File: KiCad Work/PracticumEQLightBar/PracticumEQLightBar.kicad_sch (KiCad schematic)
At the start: 57 parts, among them J1 AudioJack3Pin, U1 TEENSY 4.1, U2 TEENSY AUDIO ADAPTER BOARD RE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, U4 SN74AHCT125N

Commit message: Added unified power, caps, Data in resistor. Modified placements to match enclosure I/O git status
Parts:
- removed TP1, TP2: TestPoint_Alt, TestPoint:TestPoint_Pad_1.5x1.5mm, symbol Connector:TestPoint_Alt
- added C1: 470u, Capacitor_THT:CP_Radial_D8.0mm_P3.80mm, symbol Device:C_Small_US
- added C2: 0.1u, Capacitor_THT:C_Disc_D4.7mm_W2.5mm_P5.00mm, symbol Device:C_Small
- added J2: 5V, 4A DC, EQLightBarLibrary:PJ047BH DC Jack, symbol Connector:Barrel_Jack_Switch
- added R1: 330, Resistor_THT:R_Axial_DIN0207_L6.3mm_D2.5mm_P7.62mm_Horizontal, symbol Device:R_Small
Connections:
- net 3.3V DATA: now also U4.2 (1A); no longer U4.5 (2A)
- net CLOCK: now also U4.5 (2A); no longer U4.2 (1A)
- net GND: now also U1.GND1 (GND), U1.GND3 (GND__2), U2.G, U2.GND, C1.2, C2.2, J2.2, J2.3
- net at D1.1 (DI): now also R1.2; no longer U4.6 (2Y)
- net at D1.2 (CI): now also U4.6 (2Y); no longer U4.3 (1Y)
- net 5V USB renamed 5V DC
- net 5V DC: now also C1.1, C2.1, J2.1
- new net: R1.1, U4.3 (1Y)

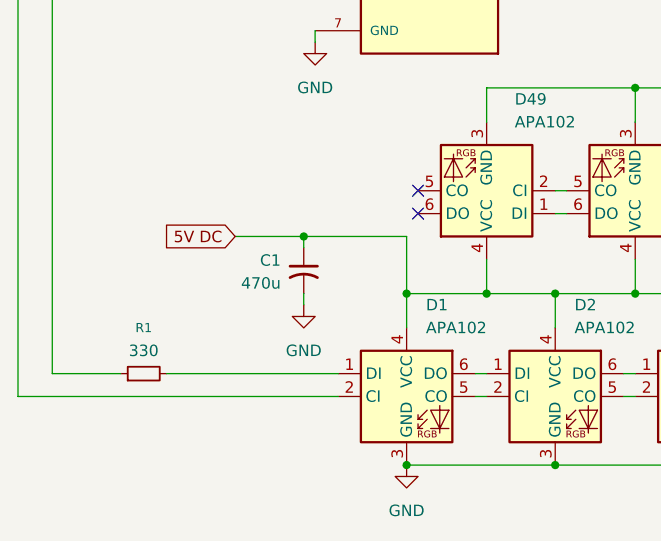
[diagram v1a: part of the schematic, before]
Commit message: DC jack changed to 2.1mm
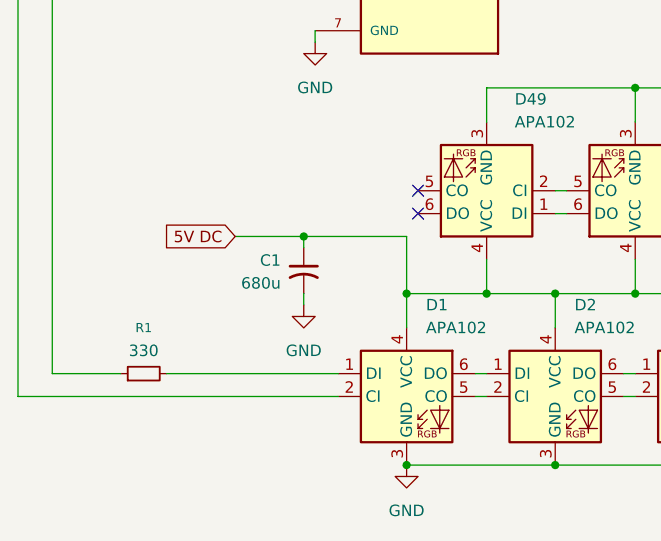
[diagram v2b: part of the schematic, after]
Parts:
- C1: value 470u -> 680u
- J2: footprint EQLightBarLibrary:PJ047BH DC Jack -> EQLightBarLibrary:694106301002_1
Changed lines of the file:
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@@
 			)
 		)
-		(property "Value" "470u"
+		(property "Value" "680u"
 			(at 68.58 189.3569 0)
 			(effects
@@
 			)
 		)
-		(property "Footprint" "EQLightBarLibrary:PJ047BH DC Jack"
+		(property "Footprint" "EQLightBarLibrary:694106301002_1"
 			(at 224.79 28.956 0)
 			(effects

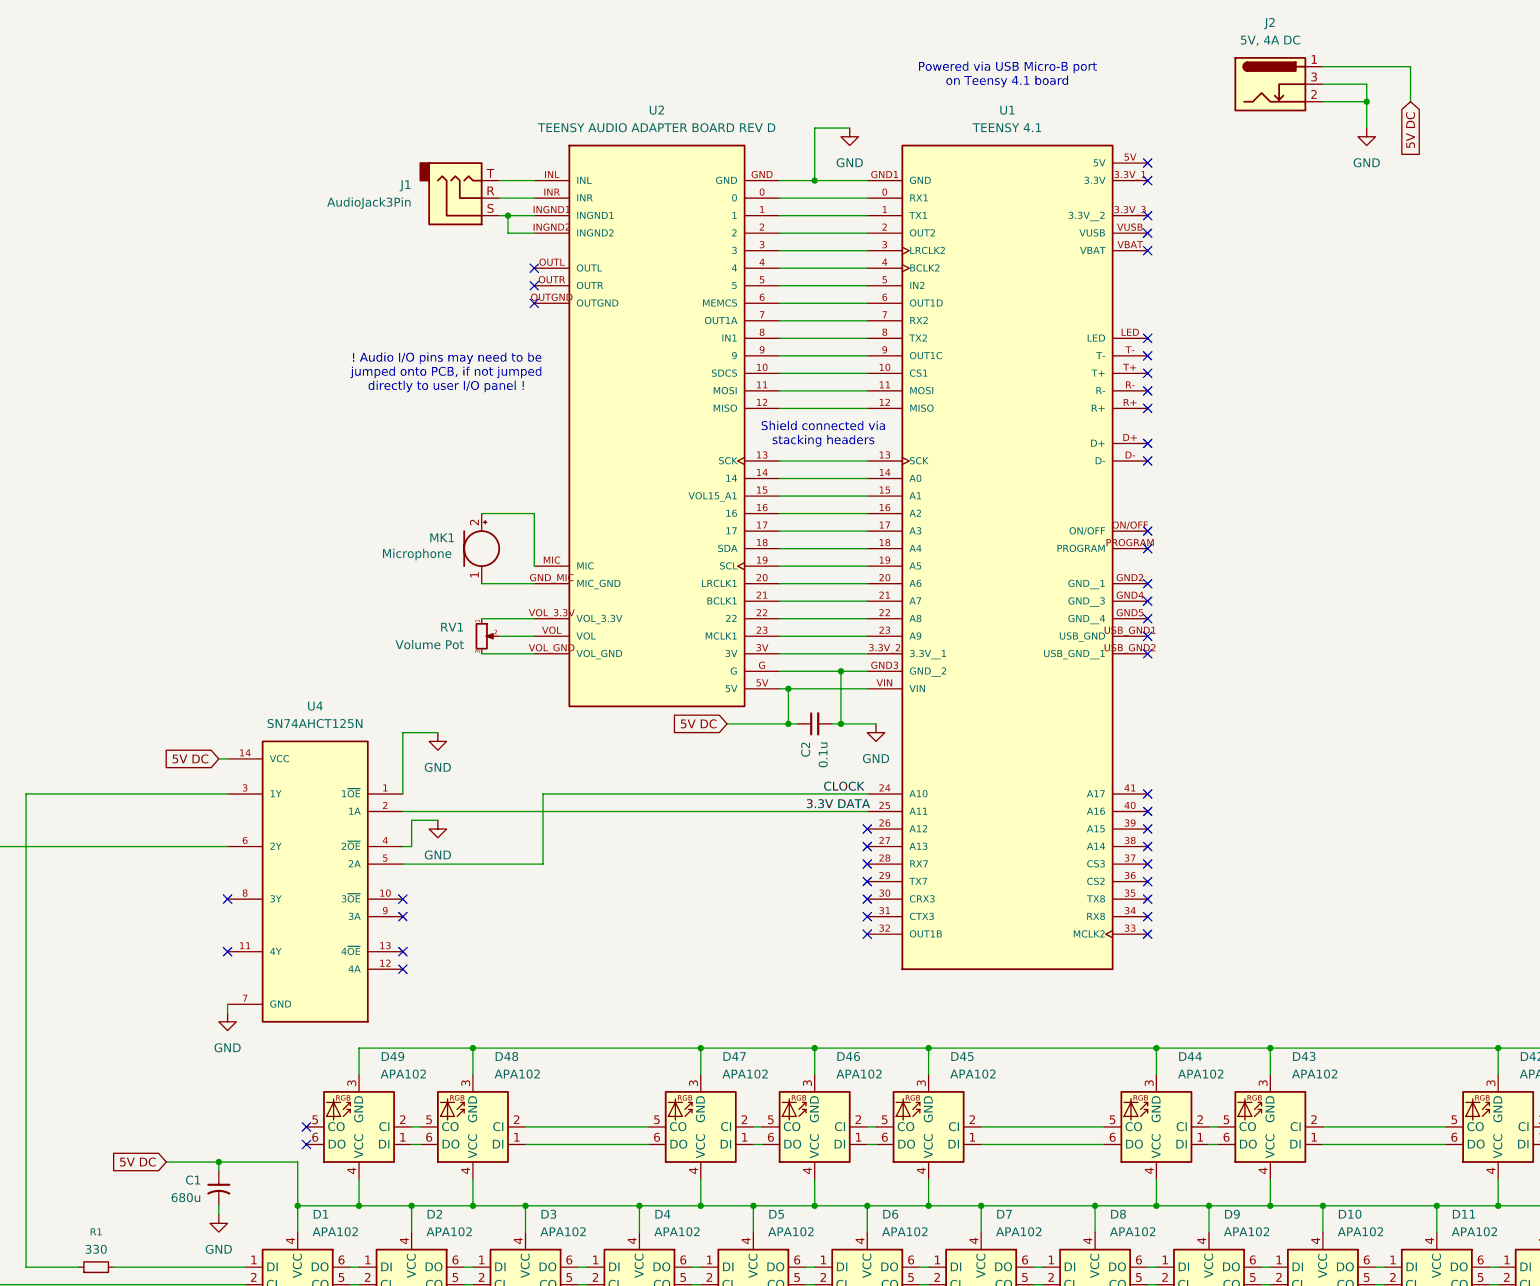
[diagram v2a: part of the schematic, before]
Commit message: Added test points
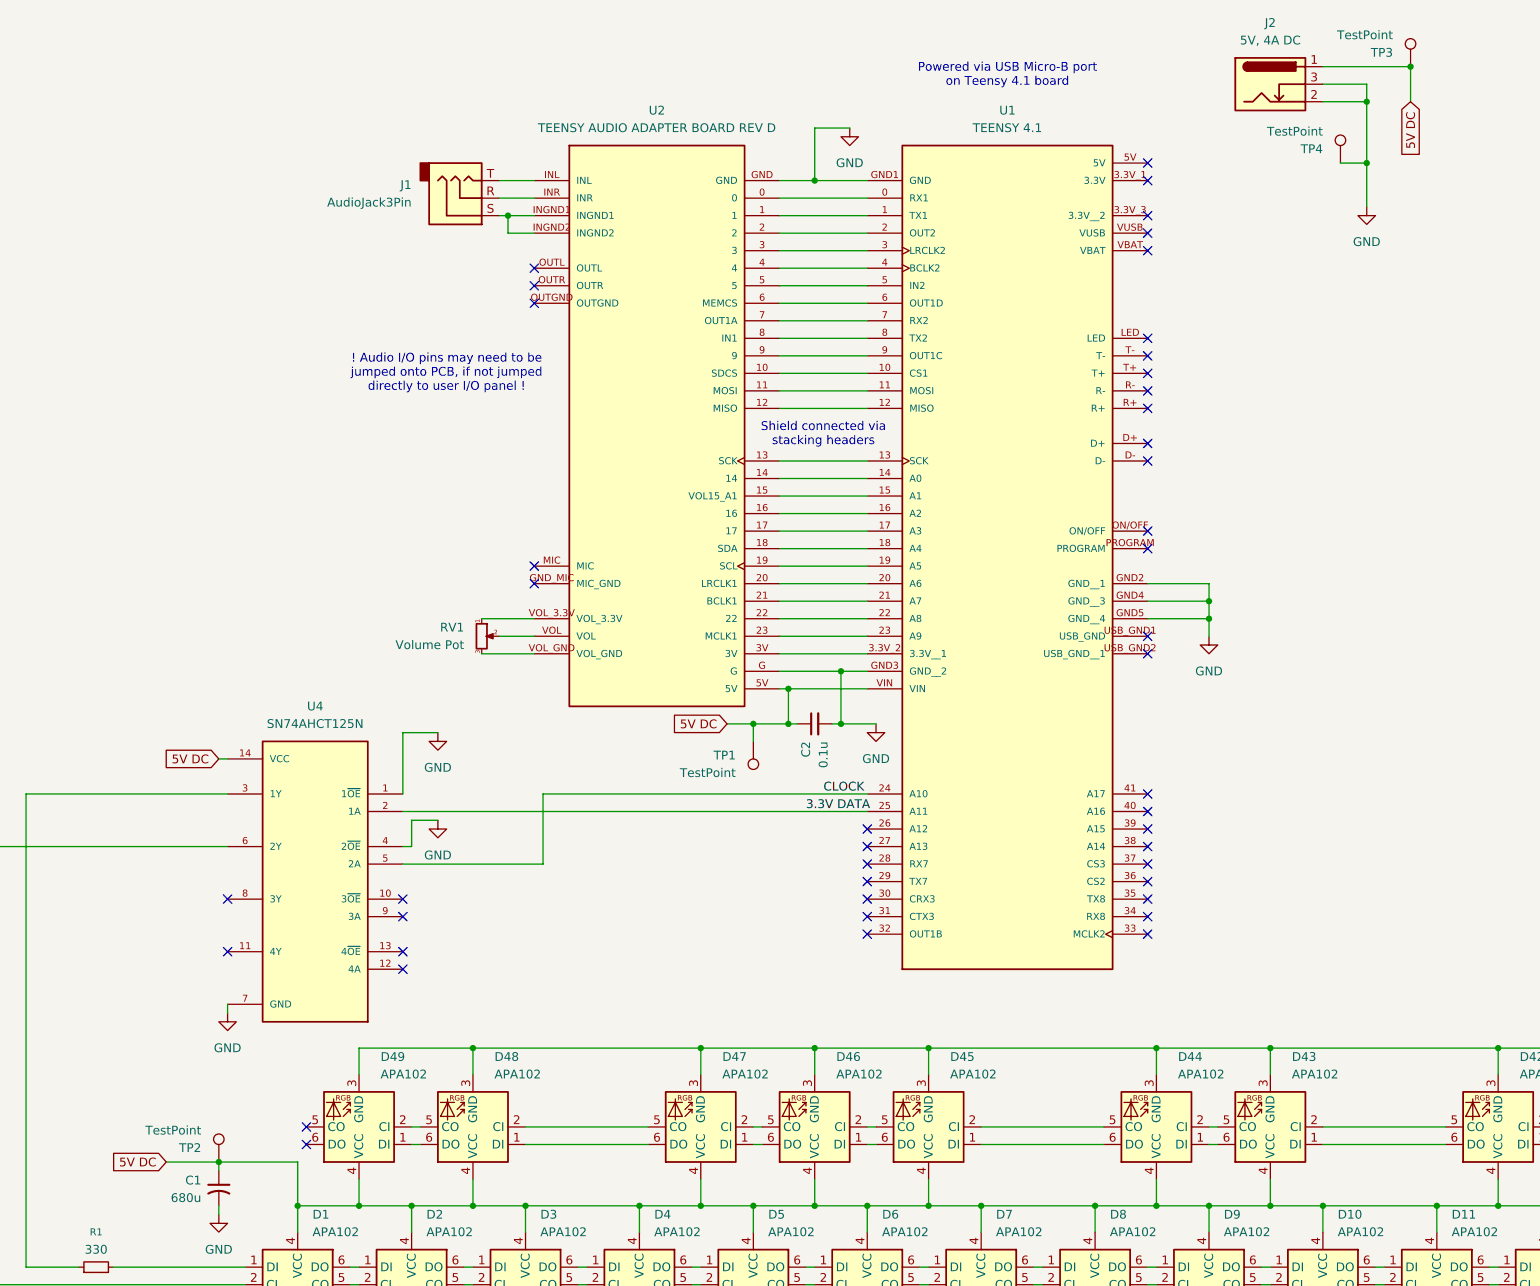
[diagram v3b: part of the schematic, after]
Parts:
- removed MK1: Microphone, symbol Device:Microphone
- added TP1, TP2, TP3, TP4: TestPoint, TestPoint:TestPoint_Pad_1.0x1.0mm, symbol Connector:TestPoint
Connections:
- net 5V DC: now also TP1.1, TP2.1, TP3.1
- net GND: now also U1.GND2 (GND__1), U1.GND4 (GND__3), U1.GND5 (GND__4), TP4.1
- no-connect marks 46 -> 45

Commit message: final PCB layout
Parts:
- removed J1: AudioJack3Pin, symbol Connector_Audio:AudioJack3
- removed RV1: Volume Pot, symbol Device:R_Potentiometer_Small
- added C3, C4: 33u, Capacitor_THT:CP_Radial_D4.0mm_P2.00mm, symbol Device:C_Small_US
- added C5: 0.5u, Capacitor_THT:C_Disc_D4.7mm_W2.5mm_P5.00mm, symbol Device:C_Small
- added C6, C7: 0.1u, Capacitor_THT:C_Disc_D4.7mm_W2.5mm_P5.00mm, symbol Device:C_Small
- added J1, J3: Conn_01x02_Socket, Connector_PinHeader_2.54mm:PinHeader_1x02_P2.54mm_Vertical, symbol Connector:Conn_01x02_Socket
- added R2: 330, Resistor_THT:R_Axial_DIN0207_L6.3mm_D2.5mm_P7.62mm_Horizontal, symbol Device:R_Small
- added RV2: R_Potentiometer, EQLightBarLibrary:PTV09A4030FA104 Pot 100k, symbol Device:R_Potentiometer
- added TP5, TP6: TestPoint, Connector_PinHeader_2.54mm:PinHeader_1x01_P2.54mm_Vertical, symbol Connector:TestPoint
- added U3: LM386, Package_DIP:DIP-8_W7.62mm, symbol Amplifier_Audio:LM386
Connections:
- net GND: now also C3.2, C6.2, C7.2, J1.1 (Pin_1), J3.1 (Pin_1), R2.1, RV2.1, U3.2 (-), U3.4 (GND)
- net at U2.INGND1: no longer U2.INGND2
- net at D1.2 (CI), U4.6 (2Y): now also TP6.1
- net at R1.1, U4.3 (1Y): now also TP5.1
- net 3.3V DATA renamed SDA
- net 5V DC renamed +5V
- net +5V: now also C3.1, C6.1, C7.1, U3.6 (V+)
- net CLOCK renamed SCL
- new net: C5.2, R2.2
- new net: C4.1, C5.1, U3.5
- new net: C4.2, J1.2 (Pin_2)
- new net: RV2.2, U3.3 (+)
- new net: J3.2 (Pin_2), RV2.3
- no-connect marks 45 -> 55
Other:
- note removed: "! Audio I/O pins may need to be jumped onto PCB, if not jumped directly to user I/O panel !"
- moved on the sheet: C1, C2, D1, D10, D11, D12, D13, D14, D15, D16, D17, D18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

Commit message: Drawing sheets updated with final PCB design
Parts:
- renumbered RV2 to RV1
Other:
- note added: "Audio Passthrough Amp"
- note added: "Jumper from Audio Shield line out"
- note added: "LEDs and Logic Shifter"
- note added: "MCU and ADC board"
- note added: "Output to enclosure mounted speaker"
- note added: "Power In"
- note removed: "Powered via USB Micro-B port on Teensy 4.1 board"
- moved on the sheet: C1, C2, C3, C4, C5, C6, C7, D1, D10, D11, D12, D13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
